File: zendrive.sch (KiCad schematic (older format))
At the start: 8 parts

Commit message: Board complete
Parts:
- added BT1: BATTERY, symbol BATTERY
- added C3, C6: 470nF, symbol C
- added C4: 3.3nF, symbol C
- added C5: 100nF, symbol C
- added C7: 100pF, symbol C
- added D1, D2, D3: BAT41, symbol DIODESCH
- added J2: JACK_OUTPUT, symbol JACK_2P
- added Q1, Q2: 2N7000, TO92, symbol BS107
- added R3, R7, R8: 1K, symbol R
- added R4: 10K, symbol R
- added R5: 470K, symbol R
- added R6: 2M, symbol R
- added RV?: 10K, symbol POT
- added RV?: 500K, symbol POT
- added RV?: 50K, symbol POT
- added RV?: 100K, symbol POT
- C1: renamed from C?; value CP2 -> 100uF
- C2: renamed from C?; value CP2 -> 47uF
- J1: renamed from J?; value JACK_2P -> JACK_INPUT
- gave numbers to parts that had none: 3
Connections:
- net +9V: now also CON?.3, U1.8 (V+), U1.8 (V+)
- net GND: now also J1.2, U1.4 (V-), U1.4 (V-), C4.2, J2.1, J2.2, R6.2, RV?.3
- net V2: now also C5.1, R5.2
- net at U1.1: now also C7.1, D2.1 (A), Q1.1 (D), Q1.2 (G), R4.2, R8.1, RV?.3
- net at U1.2 (_): now also C6.1, R5.1
- net at U1.3 (+): now also C7.2, D3.1 (A), Q2.1 (D), Q2.2 (G), R7.2, RV?.1
- net at U1.5 (+): now also C4.1, RV?.2, RV?.3
- net at U1.6 (_): now also U1.7, C3.2
- net at J1.1: now also CON?.1, BT1.2 (-)
- net INPUT: now reaches J1.3
- net INPUT: now also C6.2, R6.1
- net at CON?.2: now also BT1.1 (+)
- new net: C5.2, RV?.2, RV?.3
- new net: R7.1, RV?.1
- new net: R8.2, RV?.2
- new net: D1.2 (K), Q2.3 (S)
- new net: D3.2 (K), Q1.3 (S)
- new net: D1.1 (A), D2.2 (K)
- new net: R4.1, RV?.1
- new net: C3.1, R3.2
- new net: R3.1, RV?.1
- new net OUTPUT: J2.3, RV?.2
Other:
- note added: "GAIN"
- note added: "LOG"
- note added: "TONE"
- note added: "VOICE"
- note added: "VOLUME"
- moved on the sheet: C1, C2, CON?, J1, R1, R2, U1A, U1B

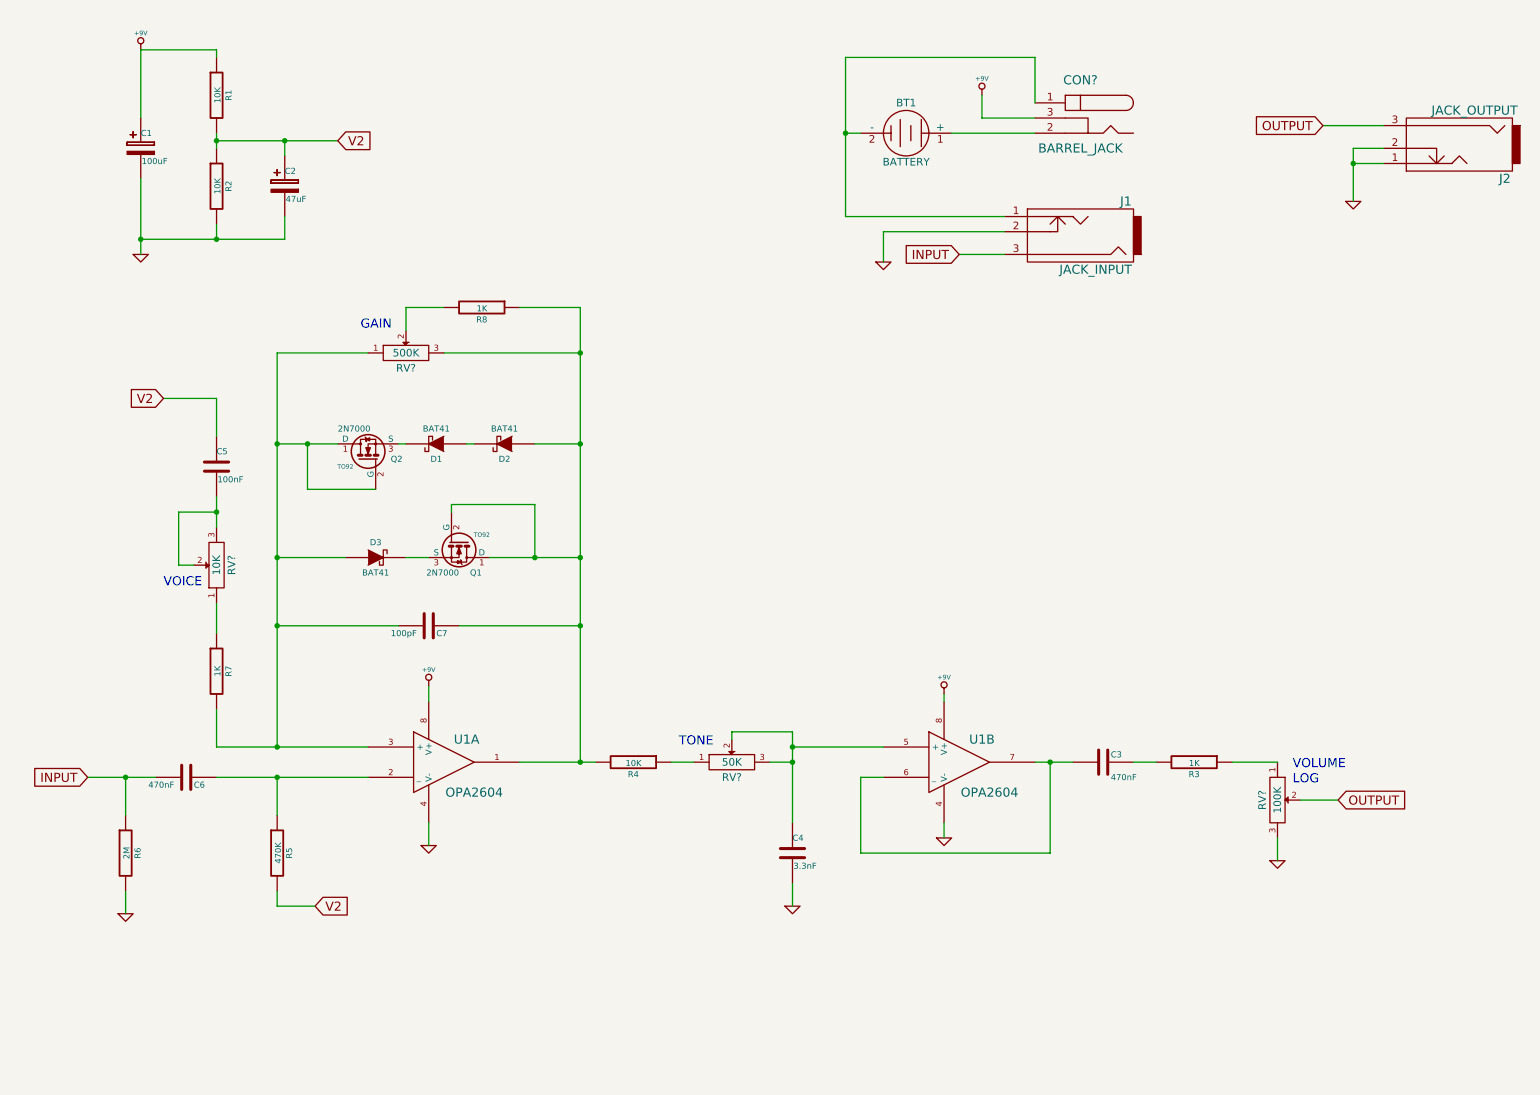
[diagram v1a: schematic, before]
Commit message: Added pot connections
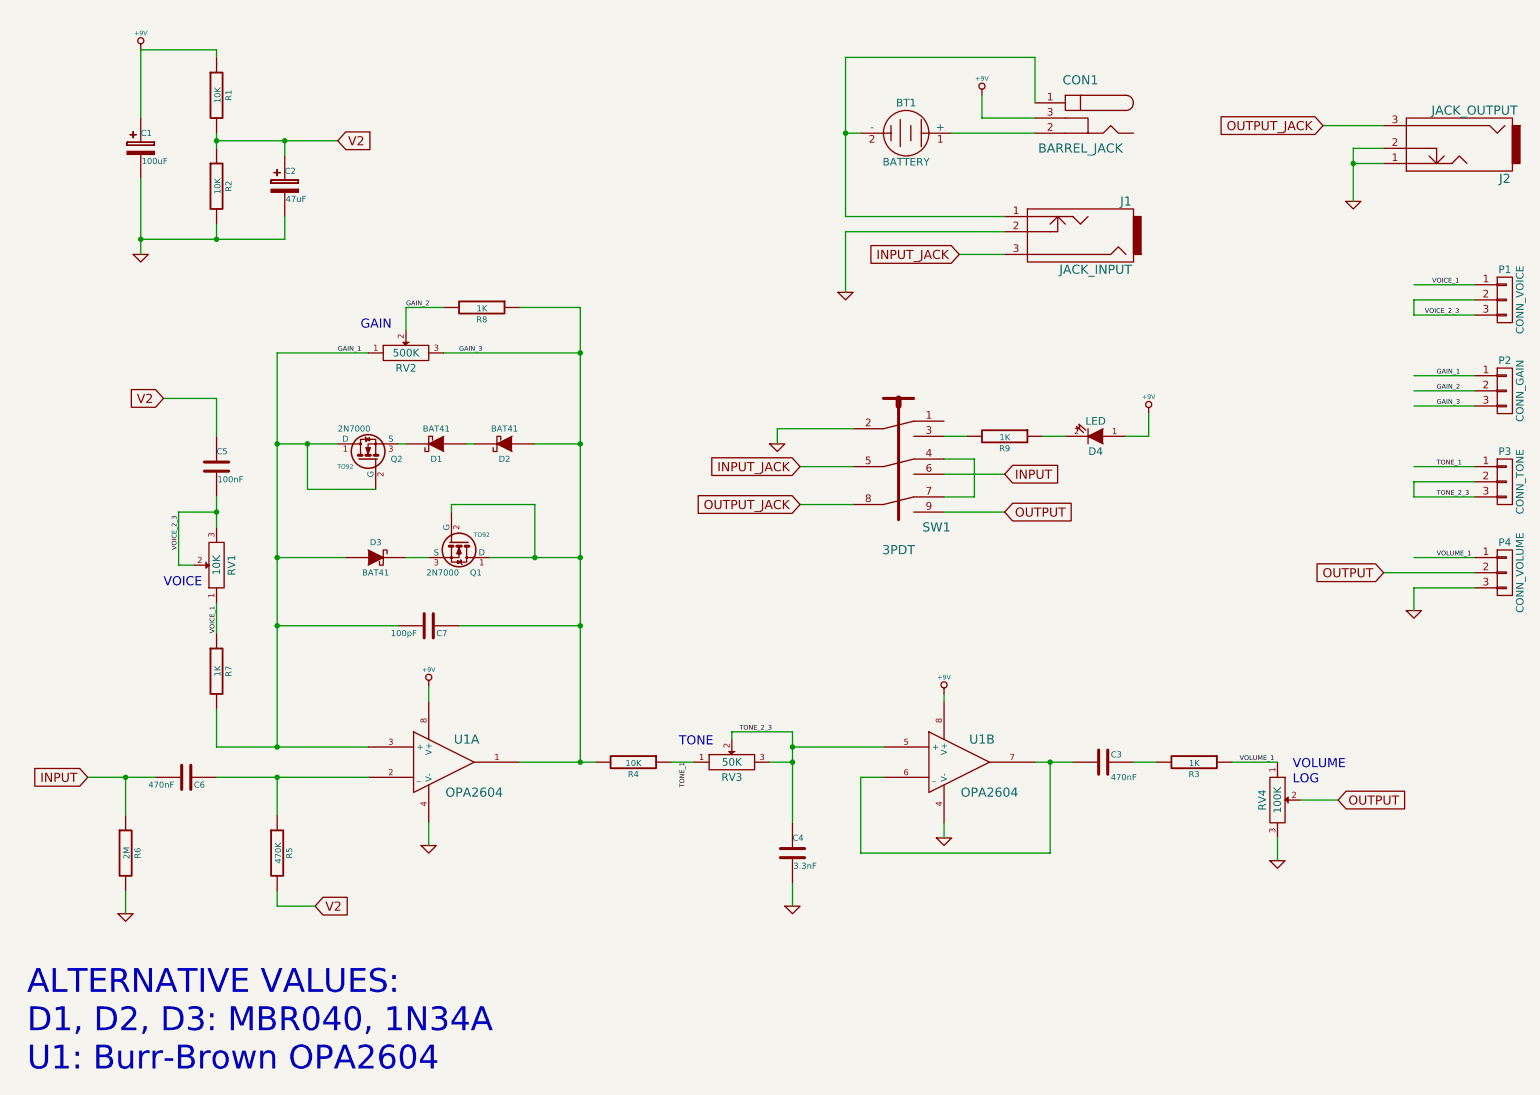
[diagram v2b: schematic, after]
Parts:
- added D4: LED, symbol LED
- added P1: CONN_VOICE, symbol CONN_01X03
- added P2: CONN_GAIN, symbol CONN_01X03
- added P3: CONN_TONE, symbol CONN_01X03
- added P4: CONN_VOLUME, symbol CONN_01X03
- added R9: 1K, symbol R
- added SW1: 3PDT, symbol 3PDT
- gave numbers to parts that had none: 5
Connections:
- net labels added: GAIN_1, GAIN_2, GAIN_3, INPUT_JACK, OUTPUT_JACK, TONE_1, TONE_2_3, VOICE_1, VOICE_2_3, VOLUME_1
- wire segments 83 -> 111
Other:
- note added: "ALTERNATIVE VALUES:\nD1, D2, D3: MBR040, 1N34A\nU1: Burr-Brown OPA2604"

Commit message: REMOVED POT CONN
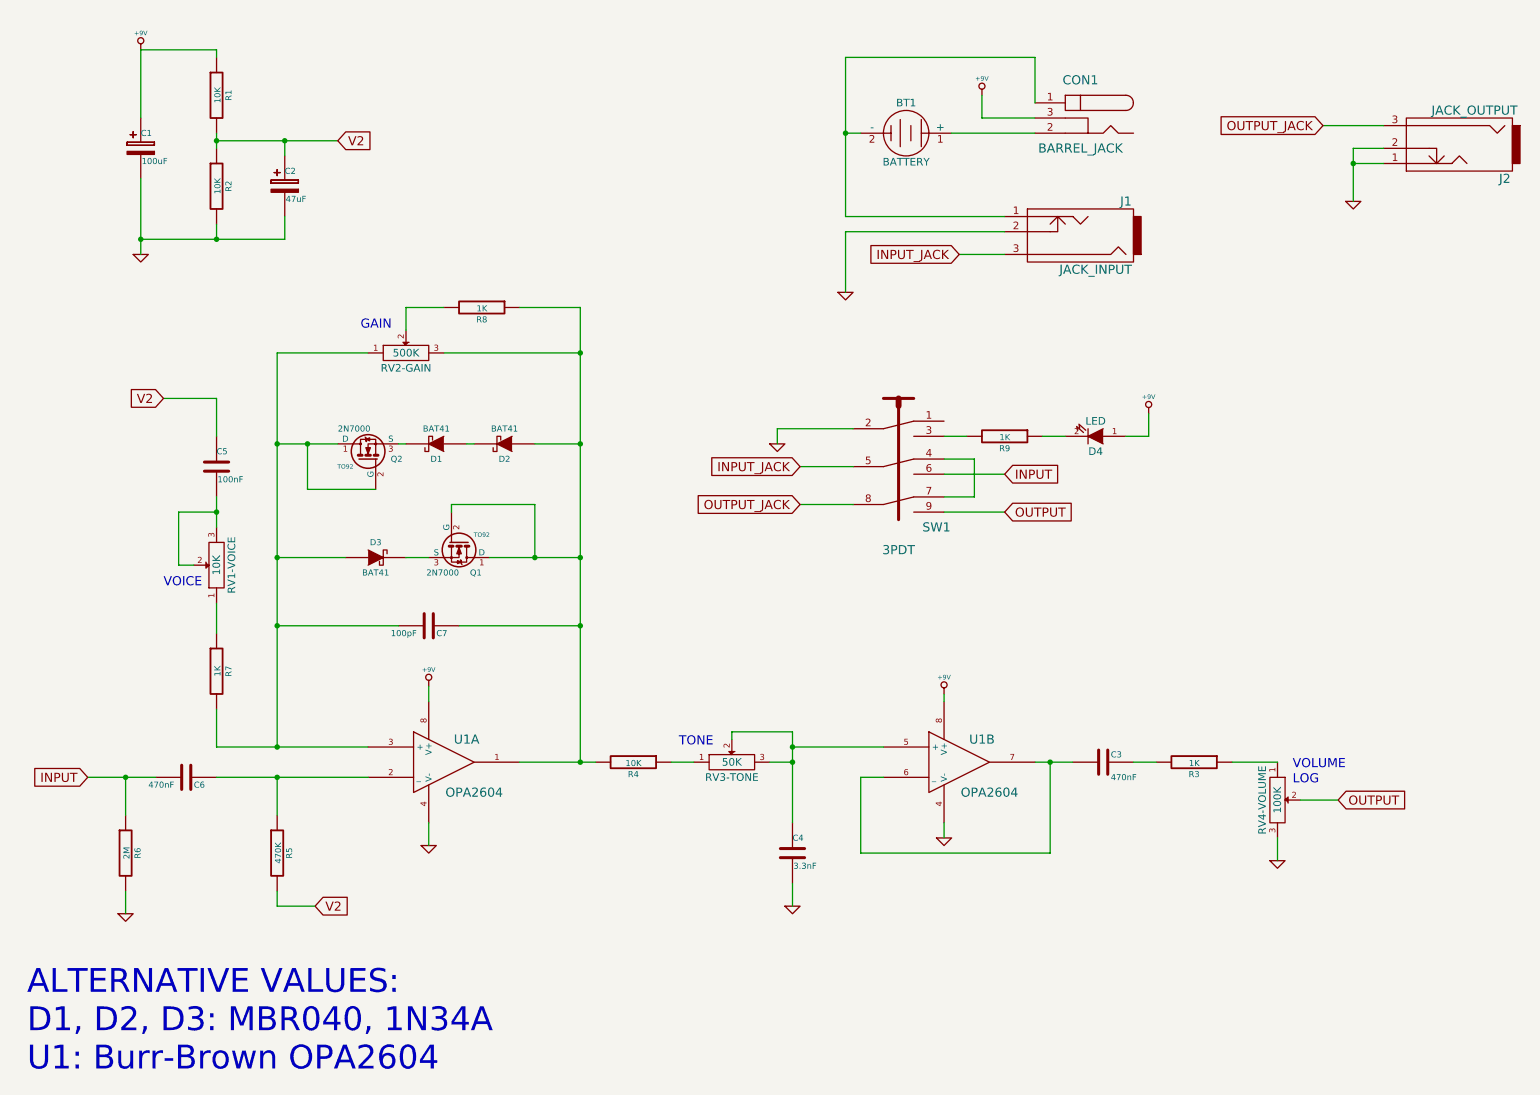
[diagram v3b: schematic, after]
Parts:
- removed P1: CONN_VOICE, symbol CONN_01X03
- removed P2: CONN_GAIN, symbol CONN_01X03
- removed P3: CONN_TONE, symbol CONN_01X03
- removed P4: CONN_VOLUME, symbol CONN_01X03
- renumbered RV1 to RV1-VOICE, RV2 to RV2-GAIN, RV3 to RV3-TONE, RV4 to RV4-VOLUME
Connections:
- net labels removed: GAIN_1, GAIN_2, GAIN_3, TONE_1, TONE_2_3, VOICE_1, VOICE_2_3, VOLUME_1
- wire segments 111 -> 96
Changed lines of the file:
@@
 $EndComp
 $Comp
-L POT RV1
+L POT RV1-VOICE
 U 1 1 54AD9D29
 P 1950 4200
-F 0 "RV1" H 1950 4100 50  0000 C CNN
+F 0 "RV1-VOICE" H 1950 4100 50  0000 C CNN
 F 1 "10K" H 1950 4200 50  0000 C CNN
 F 2 "" H 1950 4200 60  0000 C CNN
@@
 V2
 $Comp
-L POT RV2
+L POT RV2-GAIN
 U 1 1 54ADAC20
 P 3200 2800
-F 0 "RV2" H 3200 2700 50  0000 C CNN
+F 0 "RV2-GAIN" H 3200 2700 50  0000 C CNN
 F 1 "500K" H 3200 2800 50  0000 C CNN
 F 2 "" H 3200 2800 60  0000 C CNN
@@
 $EndComp
 $Comp
-L POT RV3
+L POT RV3-TONE
 U 1 1 54ADCC06
 P 5350 5500
-F 0 "RV3" H 5350 5400 50  0000 C CNN
+F 0 "RV3-TONE" H 5350 5400 50  0000 C CNN
 F 1 "50K" H 5350 5500 50  0000 C CNN
 F 2 "" H 5350 5500 60  0000 C CNN
@@
 $EndComp
 $Comp
-L POT RV4
+L POT RV4-VOLUME
 U 1 1 54ADDB89
 P 8950 5750
-F 0 "RV4" H 8950 5650 50  0000 C CNN
+F 0 "RV4-VOLUME" H 8950 5650 50  0000 C CNN
 F 1 "100K" H 8950 5750 50  0000 C CNN
 F 2 "" H 8950 5750 60  0000 C CNN
@@
 Text Notes 700  7550 0    157  ~ 0
 ALTERNATIVE VALUES:\nD1, D2, D3: MBR040, 1N34A\nU1: Burr-Brown OPA2604
-Text Label 1700 4100 1    31   ~ 0
-VOICE_2_3
-Text Label 1950 4650 1    31   ~ 0
-VOICE_1
-Text Label 2750 2800 0    31   ~ 0
-GAIN_1
-Text Label 3550 2800 0    31   ~ 0
-GAIN_3
-Text Label 3200 2500 0    31   ~ 0
-GAIN_2
-Text Label 5400 5300 0    31   ~ 0
-TONE_2_3
-Text Label 5050 5500 3    31   ~ 0
-TONE_1
-$Comp
-L CONN_01X03 P1
-U 1 1 54ADF759
-P 10450 2450
-F 0 "P1" H 10450 2650 50  0000 C CNN
-F 1 "CONN_VOICE" V 10550 2450 50  0000 C CNN
-F 2 "" H 10450 2450 60  0000 C CNN
-F 3 "" H 10450 2450 60  0000 C CNN
-	1    10450 2450
-	1    0    0    -1
-$EndComp
-$Comp
-L CONN_01X03 P2
-U 1 1 54ADF7B8
-P 10450 3050
-F 0 "P2" H 10450 3250 50  0000 C CNN
-F 1 "CONN_GAIN" V 10550 3050 50  0000 C CNN
-F 2 "" H 10450 3050 60  0000 C CNN
-F 3 "" H 10450 3050 60  0000 C CNN
-	1    10450 3050
-	1    0    0    -1
-$EndComp
-$Comp
-L CONN_01X03 P3
-U 1 1 54ADF7F1
-P 10450 3650
-F 0 "P3" H 10450 3850 50  0000 C CNN
-F 1 "CONN_TONE" V 10550 3650 50  0000 C CNN
-F 2 "" H 10450 3650 60  0000 C CNN
-F 3 "" H 10450 3650 60  0000 C CNN
-	1    10450 3650
-	1    0    0    -1
-$EndComp
-$Comp
-L CONN_01X03 P4
-U 1 1 54ADF82C
-P 10450 4250
-F 0 "P4" H 10450 4450 50  0000 C CNN
-F 1 "CONN_VOLUME" V 10550 4250 50  0000 C CNN
-F 2 "" H 10450 4250 60  0000 C CNN
-F 3 "" H 10450 4250 60  0000 C CNN
-	1    10450 4250
-	1    0    0    -1
-$EndComp
-Wire Wire Line
-	10250 2350 9850 2350
-Wire Wire Line
-	10250 2450 9850 2450
-Wire Wire Line
-	10250 2550 9850 2550
-Wire Wire Line
-	9850 2550 9850 2450
-Text Label 10150 2550 2    31   ~ 0
-VOICE_2_3
-Text Label 10150 2350 2    31   ~ 0
-VOICE_1
-Wire Wire Line
-	10250 2950 9850 2950
-Wire Wire Line
-	10250 3050 9850 3050
-Wire Wire Line
-	10250 3150 9850 3150
-Text Label 10000 2950 0    31   ~ 0
-GAIN_1
-Text Label 10000 3050 0    31   ~ 0
-GAIN_2
-Text Label 10000 3150 0    31   ~ 0
-GAIN_3
-Wire Wire Line
-	10250 3650 9850 3650
-Wire Wire Line
-	9850 3650 9850 3750
-Wire Wire Line
-	9850 3750 10250 3750
-Wire Wire Line
-	10250 3550 9850 3550
-Text Label 10000 3550 0    31   ~ 0
-TONE_1
-Text Label 10000 3750 0    31   ~ 0
-TONE_2_3
-Text GLabel 9650 4250 0    60   Input ~ 0
-OUTPUT
-Wire Wire Line
-	10250 4250 9650 4250
-Wire Wire Line
-	10250 4150 9850 4150
-Wire Wire Line
-	10250 4350 9850 4350
-Text Label 8700 5500 0    31   ~ 0
-VOLUME_1
-Text Label 10000 4150 0    31   ~ 0
-VOLUME_1
-$Comp
-L GND #PWR?
-U 1 1 54AE323E
-P 9850 4500
-F 0 "#PWR?" H 9850 4500 30  0001 C CNN
-F 1 "GND" H 9850 4430 30  0001 C CNN
-F 2 "" H 9850 4500 60  0000 C CNN
-F 3 "" H 9850 4500 60  0000 C CNN
-	1    9850 4500
-	1    0    0    -1
-$EndComp
-Wire Wire Line
-	9850 4350 9850 4500
 $EndSCHEMATC

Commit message: Adding footprints
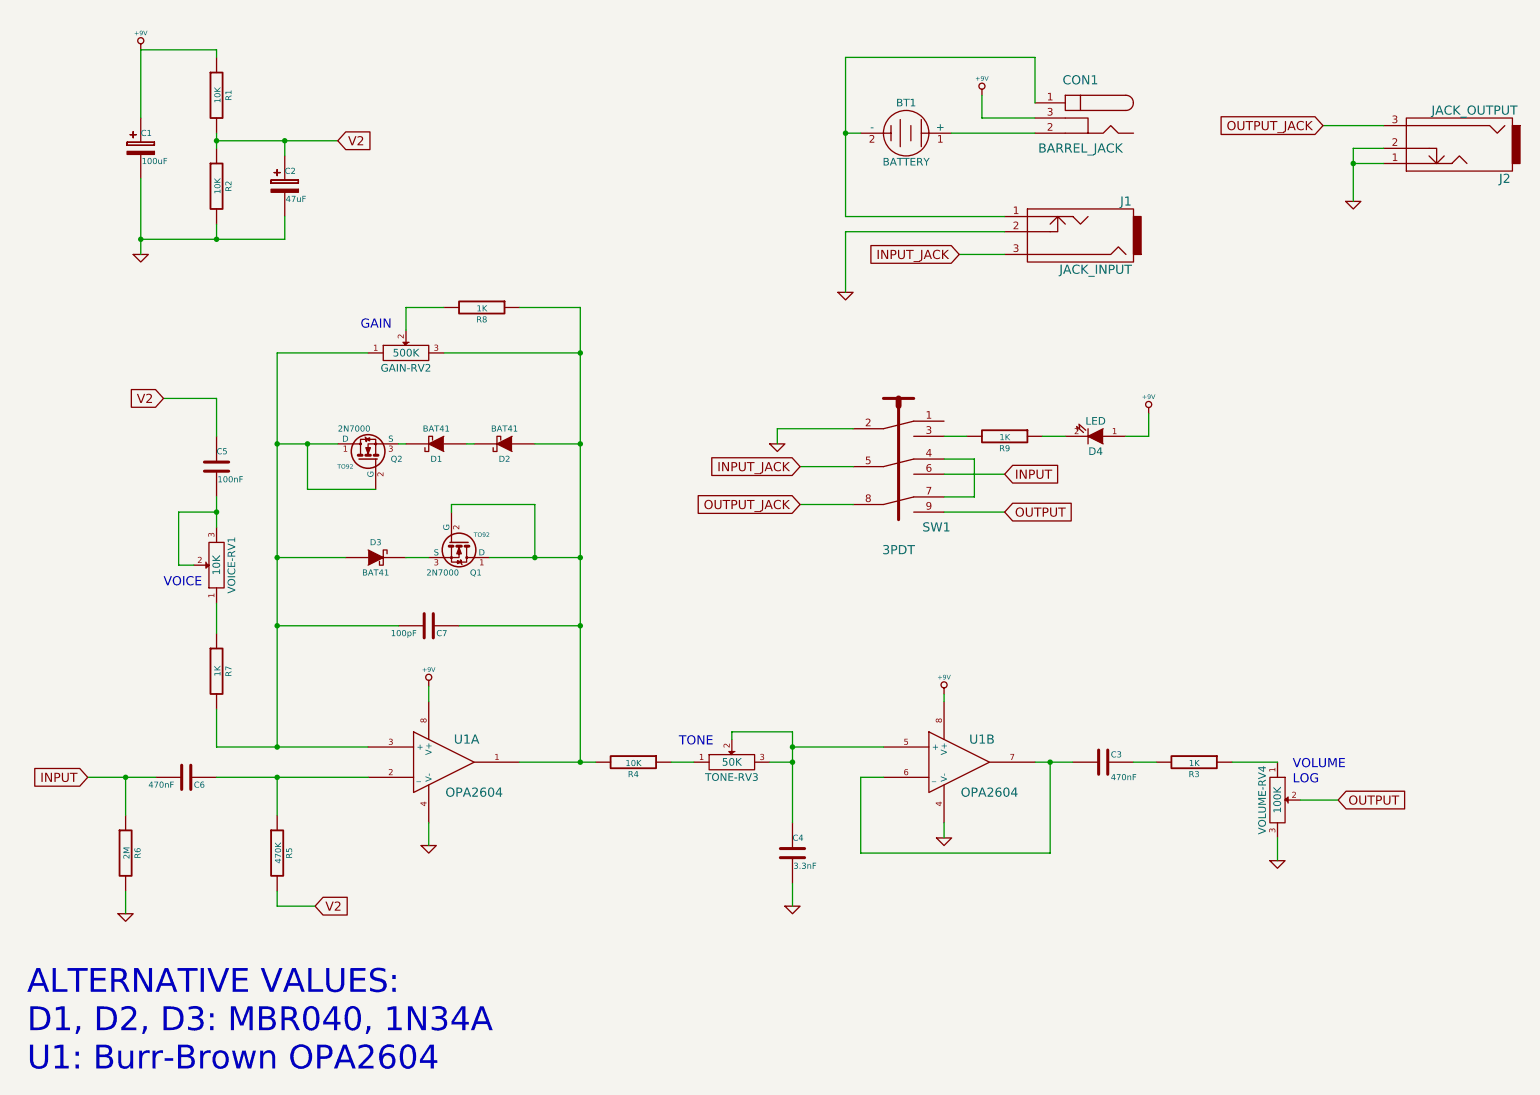
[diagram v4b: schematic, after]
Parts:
- renumbered RV2-GAIN to GAIN-RV2, RV3-TONE to TONE-RV3, RV1-VOICE to VOICE-RV1, RV4-VOLUME to VOLUME-RV4
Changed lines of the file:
@@
 $EndComp
 $Comp
-L POT RV1-VOICE
+L POT VOICE-RV1
 U 1 1 54AD9D29
 P 1950 4200
-F 0 "RV1-VOICE" H 1950 4100 50  0000 C CNN
+F 0 "VOICE-RV1" H 1950 4100 50  0000 C CNN
 F 1 "10K" H 1950 4200 50  0000 C CNN
 F 2 "" H 1950 4200 60  0000 C CNN
@@
 V2
 $Comp
-L POT RV2-GAIN
+L POT GAIN-RV2
 U 1 1 54ADAC20
 P 3200 2800
-F 0 "RV2-GAIN" H 3200 2700 50  0000 C CNN
+F 0 "GAIN-RV2" H 3200 2700 50  0000 C CNN
 F 1 "500K" H 3200 2800 50  0000 C CNN
 F 2 "" H 3200 2800 60  0000 C CNN
@@
 $EndComp
 $Comp
-L POT RV3-TONE
+L POT TONE-RV3
 U 1 1 54ADCC06
 P 5350 5500
-F 0 "RV3-TONE" H 5350 5400 50  0000 C CNN
+F 0 "TONE-RV3" H 5350 5400 50  0000 C CNN
 F 1 "50K" H 5350 5500 50  0000 C CNN
 F 2 "" H 5350 5500 60  0000 C CNN
@@
 $EndComp
 $Comp
-L POT RV4-VOLUME
+L POT VOLUME-RV4
 U 1 1 54ADDB89
 P 8950 5750
-F 0 "RV4-VOLUME" H 8950 5650 50  0000 C CNN
+F 0 "VOLUME-RV4" H 8950 5650 50  0000 C CNN
 F 1 "100K" H 8950 5750 50  0000 C CNN
 F 2 "" H 8950 5750 60  0000 C CNN

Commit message: Update
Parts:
- Q1, Q2: footprint TO92 -> Discret:TO92
